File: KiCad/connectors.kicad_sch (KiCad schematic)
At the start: 1 part, among them J3 FTSH-107-01-L-DV-K

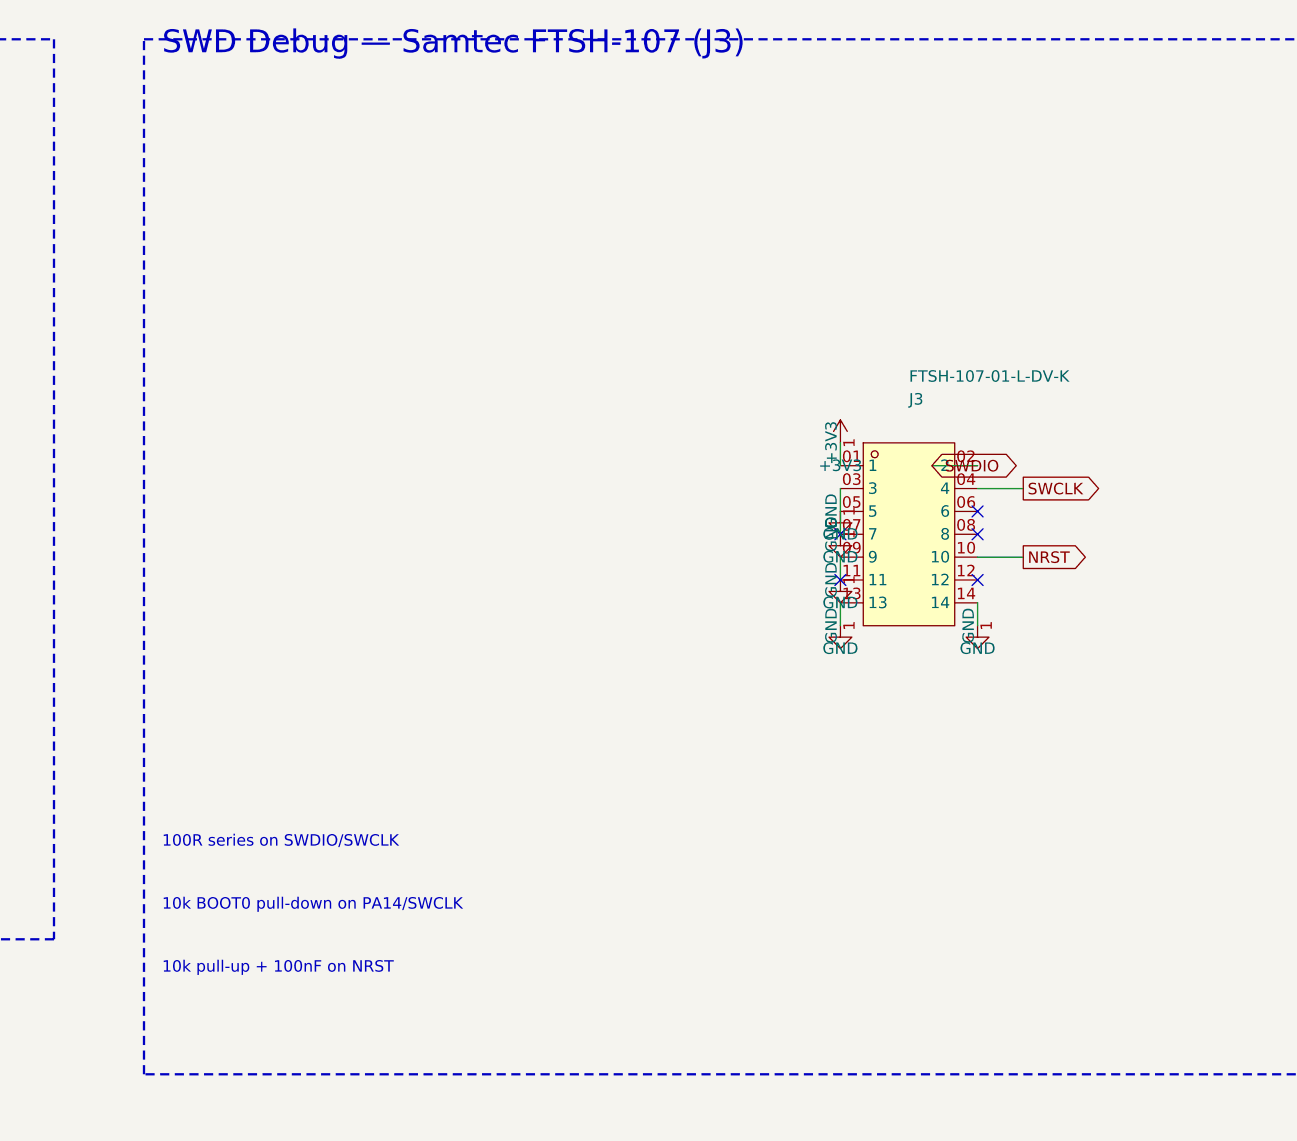
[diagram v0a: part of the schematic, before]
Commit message: Schematics edited manually
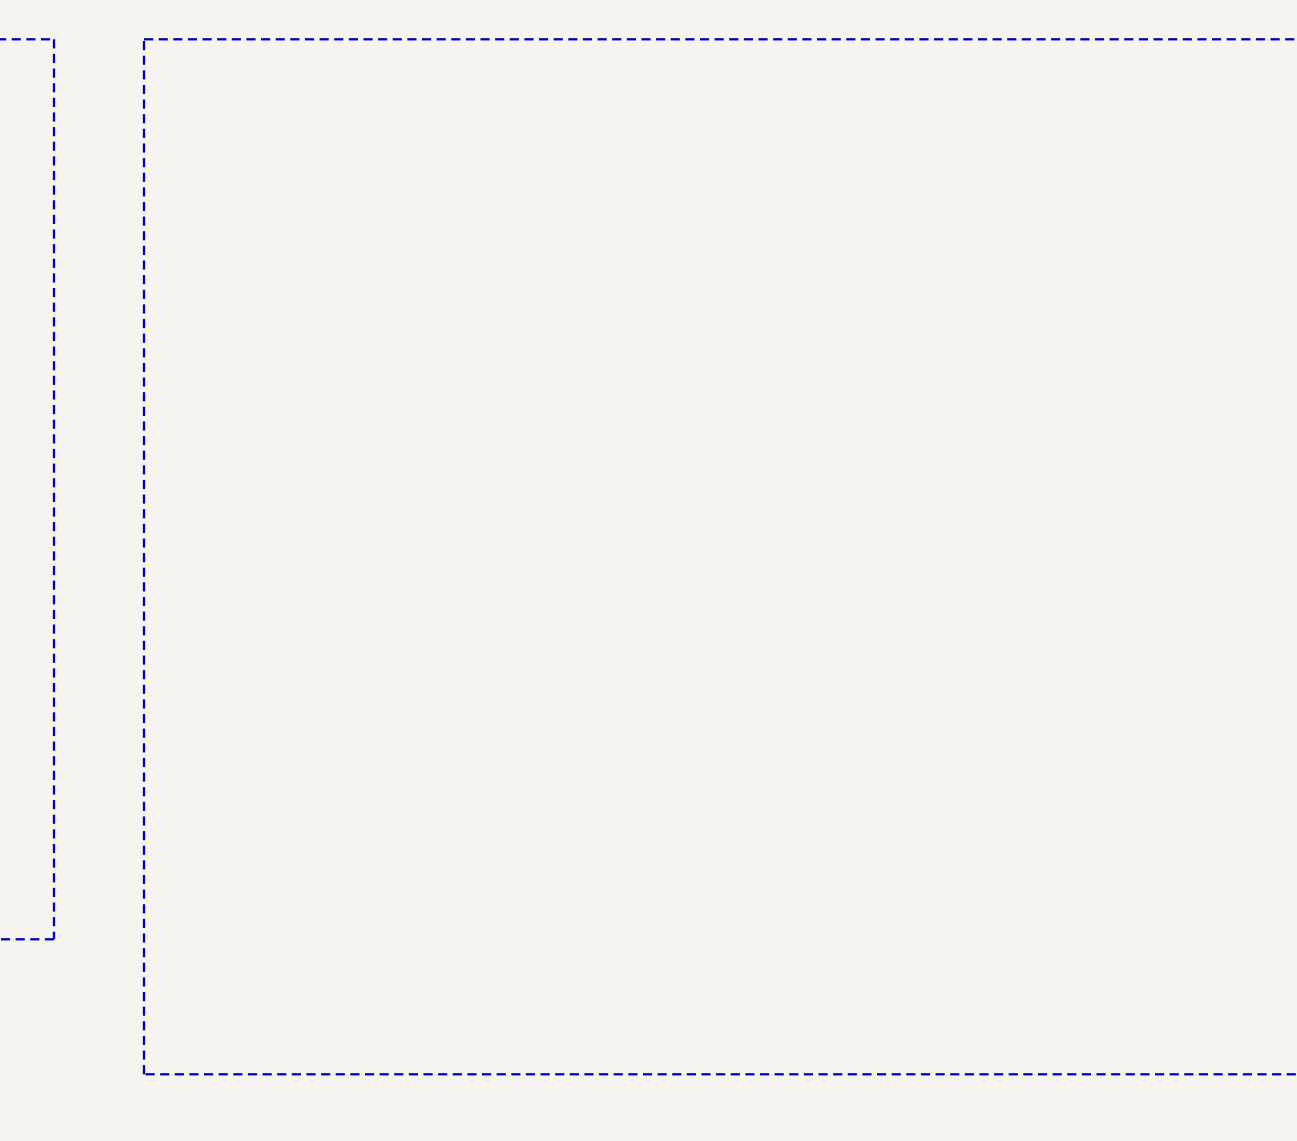
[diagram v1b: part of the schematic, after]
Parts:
- removed J3: FTSH-107-01-L-DV-K, sldrnrd:HDR-SMD_14P-P1.27_FTSH-107-01-L-DV-K, symbol sldrnrd:Connector/100Mil/FTSH-107-01-L-DV-K
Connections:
- no-connect marks 5 -> 0
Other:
- note removed: "100R series on SWDIO/SWCLK"
- note removed: "10k BOOT0 pull-down on PA14/SWCLK"
- note removed: "10k pull-up + 100nF on NRST"
- note removed: "SWD Debug — Samtec FTSH-107 (J3)"

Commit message: Schematic finalized
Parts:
- added C37, C38: 100n, sldrnrd:C_0603, symbol sldrnrd:Capacitor/C_0603
- added J2: USB-C, sldrnrd:USB_C, symbol sldrnrd:Connector/USB/USB_C
- added J3: Header_FFC_1.0mm_06, sldrnrd:Header_FFC_1.0mm_06, symbol sldrnrd:Connector/FFC/Header_FFC_1.0mm_06
- added J4: Header_50mil_2x07, sldrnrd:Header_50mil_2x07, symbol sldrnrd:Connector/50Mil/Header_50mil_2x07
- added J5, J6: Header_FFC_1.0mm_10, sldrnrd:Header_FFC_1.0mm_10, symbol sldrnrd:Connector/FFC/Header_FFC_1.0mm_10
- added R26, R28: 5k1, sldrnrd:R_0603, symbol sldrnrd:Resistor/R_0603
- added R27, R30: 100k, sldrnrd:R_0603, symbol sldrnrd:Resistor/R_0603
- added R29: 68k, sldrnrd:R_0603, symbol sldrnrd:Resistor/R_0603
- added R31: 33k, sldrnrd:R_0603, symbol sldrnrd:Resistor/R_0603
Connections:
- net GND: now also C37.2, C38.2, J2.A1B12 (GND), J2.B1A12 (GND), J3.6, J4.05 (5), J4.07 (7), J4.11, J4.13, J4.14, J5.2, J6.2, R26.2, R27.2, R28.2, R30.2
- net VBUS_SENSE: now also R29.2, R30.1
- new net: C37.1, J2.1 (SHIELD), J2.2 (SHIELD), J2.3 (SHIELD), J2.4 (SHIELD), R27.1
- new net: J2.A5 (CC1), R26.1
- new net: J2.B5 (CC2), R28.1
- new net 3V3: J3.1, J4.03 (3), J5.4, J5.6, J6.4, J6.6, R31.1
- new net DEBUG_UART_MCU_TO_PC: J4.02 (2)
- new net DEBUG_UART_PC_TO_MCU: J4.01 (1)
- new net PCAP04_1_INT: J5.10
- new net PCAP04_1_P2: J5.9
- new net PCAP04_1_P3: J5.8
- new net PCAP04_1_SCL: J5.1
- new net PCAP04_1_SDA: J5.3
- new net PCAP04_2_INT: J6.10
- new net PCAP04_2_P2: J6.9
- new net PCAP04_2_P3: J6.8
- new net PCAP04_2_SCL: J6.1
- new net PCAP04_2_SDA: J6.3
- new net SCL3300_CS: J3.2
- new net SCL3300_MISO: J3.4
- new net SCL3300_MOSI: J3.5
- new net SCL3300_SCK: J3.3
- new net SWCLK: J4.06 (6)
- new net SWDIO: J4.04 (4)
- new net SWO: J4.08 (8)
- new net USB_D+: J2.A7 (D+), J2.B6 (D+)
- new net USB_D-: J2.A6 (D-), J2.B7 (D-)
- new net V_USB: J2.A4B9 (VBUS), J2.B4A9 (VBUS), R29.1
- new net ~{RST}: C38.1, J4.12, R31.2
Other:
- note added: "Capacitance Sensor 1 PCAP04"
- note added: "Capacitance Sensor 2 PCAP04"
- note added: "Debug / Program"
- note added: "Inclination Sensor SCL3300"
- note removed: "22R series on D+/D-"
- note removed: "CC1/CC2: 5.1k to GND"
- note removed: "Daughter Board FFC Connectors (6-pin, 1.0mm pitch)"
- note removed: "J5 — SCL3300 (SPI2)"
- note removed: "J6 — PCAP04 #1 (I2C1)"
- note removed: "J7 — PCAP04 #2 (I2C2)"
- note removed: "Optional VBUS detect"
- note removed: "Pin 1"
- note removed: "Pin 2"
- note removed: "Pin 3"
- note removed: "Pin 4"
- note removed: "Pin 5"
- note removed: "Pin 6"
- note removed: "USB-C SMD Receptacle"
